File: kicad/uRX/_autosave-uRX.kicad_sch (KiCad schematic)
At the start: 109 parts, among them J1 RF_GMD, J2 C165948, J3 AudioJack2_Ground, J4 +5Vfiltered, J5 +5V, J6 U.FL, J7 +3.3Vfiltered, J9 RF_In, Q1 BC847, SW1 RotaryEncoder_Switch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

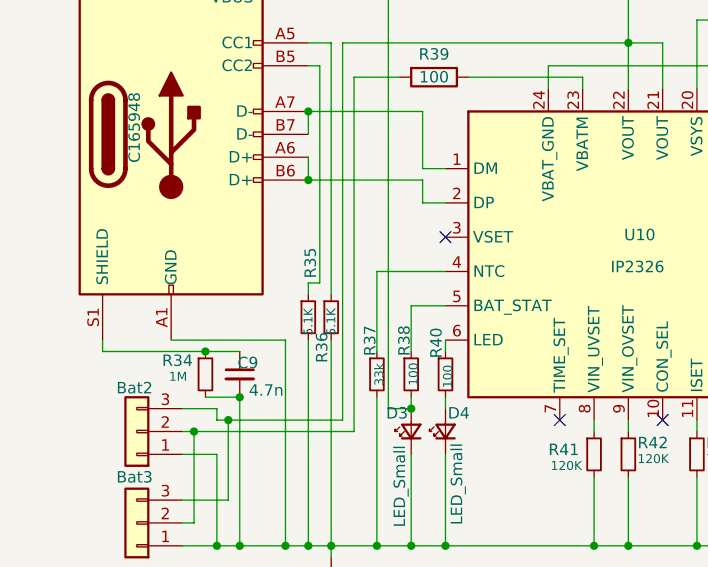
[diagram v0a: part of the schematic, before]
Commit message: resolve missing footprints
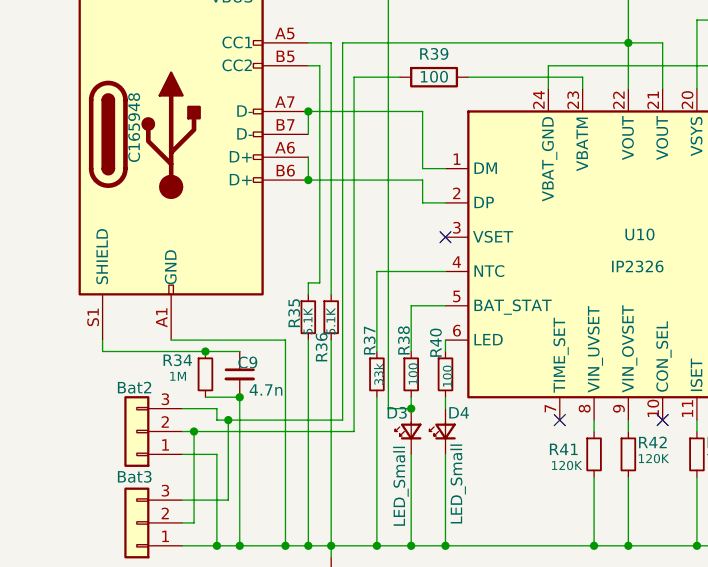
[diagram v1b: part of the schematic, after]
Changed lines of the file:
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@@
 		(dnp no)
 		(property "Reference" "R35"
-			(at 43.434 159.512 90)
+			(at 41.656 165.1 90)
 			(effects
 				(font
